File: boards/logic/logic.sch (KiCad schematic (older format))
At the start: 41 parts, among them IC1 ATTINY85-S, P1 5V_IN, P2 PROG_CONN, P3 DSPLY_CONN, Q1 Q_NPN_EBC, Q2 Q_NPN_EBC, Q3 Q_NPN_EBC, Q4 Q_NPN_EBC, Q5 Q_NPN_EBC, Q6 Q_NPN_EBC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

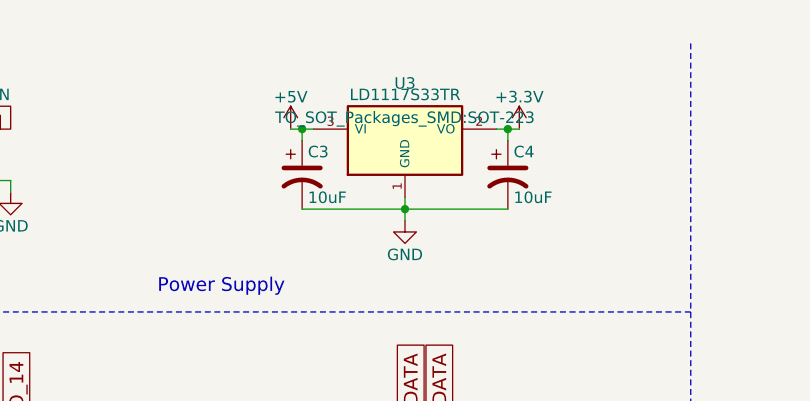
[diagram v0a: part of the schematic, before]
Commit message: Rearrange PCB layout to accomodate mounting screws.
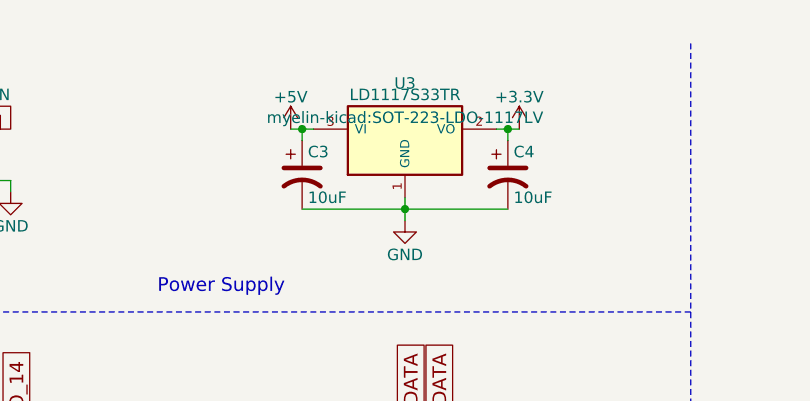
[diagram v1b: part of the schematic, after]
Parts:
- U3: footprint TO_SOT_Packages_SMD:SOT-223 -> myelin-kicad:SOT-223-LDO-1117LV
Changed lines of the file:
@@
 F 0 "U3" H 3075 1150 50  0000 C CNN
 F 1 "LD1117S33TR" H 3075 1100 50  0000 C CNN
-F 2 "TO_SOT_Packages_SMD:SOT-223" H 3075 1000 50  0000 C CNN
+F 2 "myelin-kicad:SOT-223-LDO-1117LV" H 3075 1000 50  0000 C CNN
 F 3 "" H 3075 900 50  0000 C CNN
 	1    3075 900
